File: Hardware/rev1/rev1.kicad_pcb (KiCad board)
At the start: 4 copper layers, 50 x 25 mm, 16 parts, among them J1 USB_C_Receptacle_GCT_USB4105-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, J3 TerminalBlock_MetzConnect_360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, U1 STM32F103C8Tx, U2 HT75xx-1-SOT89, U3 MS5607-02BA, U4 W25Q128JVS, Y1 16MHz

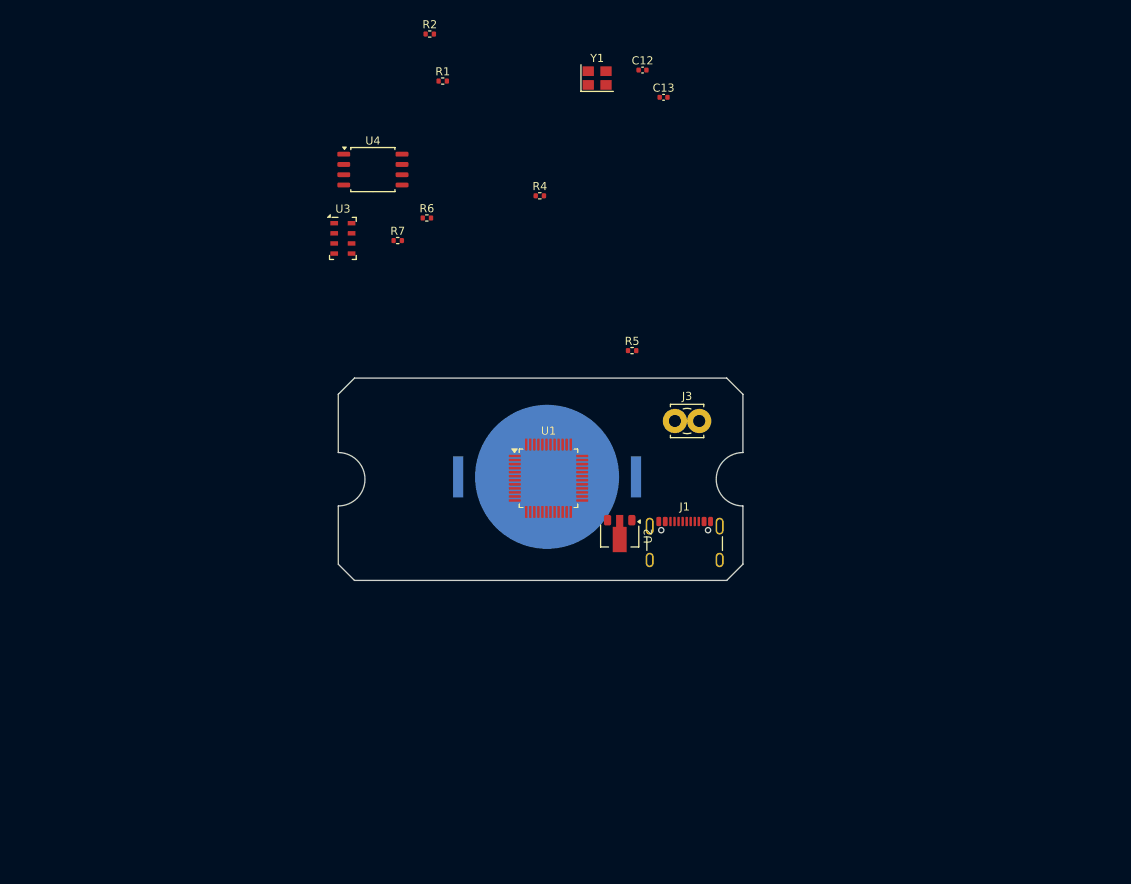
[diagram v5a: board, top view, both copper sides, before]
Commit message: Literal Progress
PCB populated, schematic changed, all pins on MCU accessible from headers, all components on board, traces required
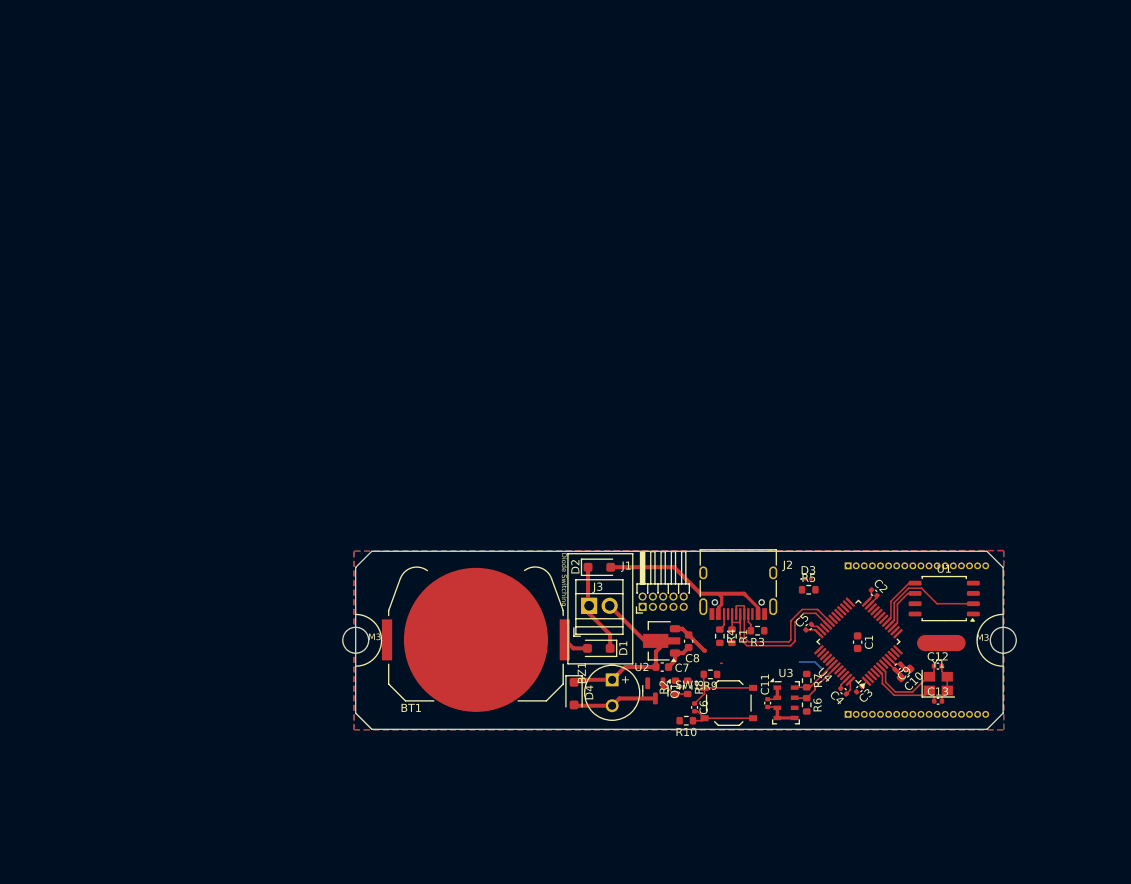
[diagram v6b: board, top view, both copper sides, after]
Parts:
- removed REF**: BatteryHolder_Keystone_3034_1x20mm, Battery:BatteryHolder_Keystone_3034_1x20mm
- added BT1: Battery_Cell, Battery:BatteryHolder_Keystone_3034_1x20mm, F.Cu at (128.0, 129.1)
- added BZ1: Buzzer, Buzzer_Beeper:MagneticBuzzer_Kingstate_KCG0601, F.Cu at (144.8, 134.1)
- added C1: 4.7u, Capacitor_SMD:C_0603_1608Metric, F.Cu at (175.2, 129.4)
- added C10: 1u, Capacitor_SMD:C_0603_1608Metric, F.Cu at (181.1, 133.3)
- added C11: 100n, Capacitor_SMD:C_0402_1005Metric, F.Cu at (164.1, 137.0)
- added C2: 100n, Capacitor_SMD:C_0402_1005Metric, F.Cu at (177.2, 123.3)
- added C3: 100n, Capacitor_SMD:C_0402_1005Metric, F.Cu at (175.4, 135.2)
- added C4: 100n, Capacitor_SMD:C_0402_1005Metric, F.Cu at (173.4, 135.5)
- added C5: 100n, Capacitor_SMD:C_0402_1005Metric, F.Cu at (169.1, 127.6)
- added C6: 100n, Capacitor_SMD:C_0402_1005Metric, F.Cu at (155.0, 137.5)
- added C7: 10u, Capacitor_SMD:C_0603_1608Metric, F.Cu at (151.0, 132.5)
- added C8: 10u, Capacitor_SMD:C_0603_1608Metric, F.Cu at (154.3, 129.3)
- added C9: 10n, Capacitor_SMD:C_0402_1005Metric, F.Cu at (180.1, 132.5)
- added D1: D, Diode_SMD:D_SOD-123F, F.Cu at (143.2, 130.2)
- added D2: D, Diode_SMD:D_SOD-123F, F.Cu at (143.3, 120.2)
- added D3: LED, LED_SMD:LED_0201_0603Metric, F.Cu at (169.1, 121.6)
- added D4: SM4007, Diode_SMD:D_SOD-123F, F.Cu at (140.1, 135.8)
- added H1: MountingHole, MountingHole:MountingHole_3.2mm_M3, F.Cu at (193.2, 129.2)
- added H2: MountingHole, MountingHole:MountingHole_3.2mm_M3, F.Cu at (113.2, 129.2)
- added J2: USB_C_Receptacle_USB2.0_14P, Connector_USB:USB_C_Receptacle_HRO_TYPE-C-31-M-12, F.Cu at (160.4, 121.9)
- added J4: Conn_01x18_Socket, Connector_PinHeader_1.00mm:PinHeader_1x18_P1.00mm_Vertical, B.Cu at (174.0, 120.0)
- added J5: Conn_01x18_Socket, Connector_PinHeader_1.00mm:PinHeader_1x18_P1.00mm_Vertical, B.Cu at (174.0, 138.3)
- added NT1: NetTie_2, NetTie:NetTie-2_SMD_Pad2.0mm, F.Cu at (185.5, 129.5)
- added Q1: AO3400A, Package_TO_SOT_SMD:SOT-23, F.Cu at (150.2, 135.4)
- added R10: 10k, Resistor_SMD:R_0603_1608Metric, F.Cu at (154.0, 139.1)
- added R3: 5k1, Resistor_SMD:R_0603_1608Metric, F.Cu at (162.8, 128.0)
- added R8: 10k, Resistor_SMD:R_0603_1608Metric, F.Cu at (154.2, 135.0)
- added R9: 1k, Resistor_SMD:R_0603_1608Metric, F.Cu at (157.0, 133.4)
- added SW1: SW_Push, Button_Switch_SMD:SW_Push_1P1T_XKB_TS-1187A, F.Cu at (159.3, 137.0)
- J1: value USB_C_Receptacle_GCT_USB4105-xx-A_16P_TopMnt_Horizontal -> Conn_ARM_JTAG_SWD_10; footprint Connector_USB:USB_C_Receptacle_GCT_USB4105-xx-A_16P_TopMnt_Horizontal -> Connector_PinHeader_1.27mm:PinHeader_2x05_P1.27mm_Horizontal
- J3: value TerminalBlock_MetzConnect_360272_1x01_Horizontal_ScrewM2.6 -> Screw_Terminal_01x02; footprint TerminalBlock_MetzConnect:TerminalBlock_MetzConnect_360272_1x01_Horizontal_ScrewM2.6 -> TerminalBlock:TerminalBlock_Xinya_XY308-2.54-2P_1x02_P2.54mm_Horizontal
- R1, R4, R6, R7: footprint Resistor_SMD:R_0402_1005Metric -> Resistor_SMD:R_0603_1608Metric
- R2: value 5k1 -> 270; footprint Resistor_SMD:R_0402_1005Metric -> Resistor_SMD:R_0603_1608Metric
- R5: value 1k5 -> 470R; footprint Resistor_SMD:R_0402_1005Metric -> Resistor_SMD:R_0603_1608Metric
- U1: value STM32F103C8Tx -> W25Q128JVS; footprint Package_QFP:LQFP-48_7x7mm_P0.5mm -> Package_SO:SOIC-8_5.23x5.23mm_P1.27mm
- U4: value W25Q128JVS -> STM32F103C8Tx; footprint Package_SO:SOIC-8_5.23x5.23mm_P1.27mm -> Package_QFP:LQFP-48_7x7mm_P0.5mm
- moved R2 86.2 mm to (152.7, 135.0), turned to 90 degrees
- moved Y1 85.9 mm to (185.1, 134.6)
- moved U4 83.7 mm to (175.3, 129.4), turned to 135 degrees
- moved C12 82.2 mm to (185.1, 132.4)
- moved C13 82.0 mm to (185.1, 136.7)
- moved U3 79.3 mm to (166.3, 136.9)
- moved R1 77.4 mm to (159.6, 128.7), turned to -90 degrees
- moved R6 76.3 mm to (168.9, 137.2), turned to 90 degrees
- moved R7 74.2 mm to (168.9, 134.2), turned to -90 degrees
- moved R4 58.8 mm to (158.1, 128.7), turned to -90 degrees
- moved U1 51.1 mm to (185.9, 124.0), turned to 180 degrees
- moved R5 36.7 mm to (169.1, 123.0)
- moved J3 25.2 mm to (142.0, 124.9)
- moved U2 13.9 mm to (150.7, 129.3), turned to 180 degrees
- moved J1 8.61 mm to (148.6, 125.1), turned to 90 degrees
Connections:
- C12 pad 1: HSE_OUT -> /Microcontroller/HSE_OUT
- C13 pad 1: HSE_IN -> /Microcontroller/HSE_IN
- J3 pad 1: (no net) -> Net-(D1-K)
- R1 pad 1: D+ -> /Microcontroller/USB.D+
- R2 pad 1: GND -> Net-(Q1-G)
- R2 pad 2: Net-(J1-CC1) -> /Microcontroller/BUZZER
- R6 pad 2: I2C2_SDA -> /Microcontroller/I2C2.SDA
- R7 pad 2: I2C2_SCK -> /Microcontroller/I2C2.SCK
- U1 pad 1: +3.3V -> unconnected-(U1-~{CS}-Pad1)
- U1 pad 2: unconnected-(U1-PC13-Pad2) -> /Microcontroller/SPI1.MISO
- U1 pad 4: unconnected-(U1-PC15-Pad4) -> GND
- U1 pad 5: HSE_IN -> /Microcontroller/SPI1.MOSI
- U1 pad 6: HSE_OUT -> /Microcontroller/SPI1.SCLK
- U1 pad 7: /MCU et al Sheet/System_Reset -> unconnected-(U1-IO3-Pad7)
- U1 pad 8: GND -> +3.3V
- U2 pad 2: Net-(J3-Pin_2) -> VBUS
- U2 pad 3: +3V3 -> +3.3V
- U3 pad 7: I2C2_SDA -> /Microcontroller/I2C2.SDA
- U3 pad 8: I2C2_SCK -> /Microcontroller/I2C2.SCK
- U4 pad 1: unconnected-(U4-~{CS}-Pad1) -> +3.3V
- U4 pad 2: Flash Data Out -> /Microcontroller/PC13
- U4 pad 3: unconnected-(U4-IO2-Pad3) -> /Microcontroller/PC14
- U4 pad 4: GND -> /Microcontroller/PC15
- U4 pad 5: Flash Data In -> /Microcontroller/HSE_IN
- U4 pad 6: SPI_CLK -> /Microcontroller/HSE_OUT
- U4 pad 7: unconnected-(U4-IO3-Pad7) -> /Microcontroller/DBG.NRESET
- U4 pad 8: +3.3V -> GND
- Y1 pad 1: HSE_IN -> /Microcontroller/HSE_IN
- Y1 pad 4: HSE_OUT -> /Microcontroller/HSE_OUT
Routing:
- net VBUS: track 0.00 -> 25.4 mm
- net VUSB: track 0.00 -> 23.9 mm
- net /Microcontroller/USB.D+: track 0.00 -> 22.8 mm
- net GND: track 0.00 -> 21.1 mm
- net /Microcontroller/USB.D-: track 0.00 -> 20.4 mm
- net /Microcontroller/SPI1.MISO: track 0.00 -> 14.3 mm
- net +3.3V: track 0.00 -> 13.5 mm
- net Net-(D1-K): track 0.00 -> 11.4 mm
- net /Microcontroller/HSE_IN: track 0.00 -> 10.6 mm
- net /Microcontroller/HSE_OUT: track 0.00 -> 10.5 mm
- net Net-(BZ1--): track 0.00 -> 10.5 mm
- net Net-(C6-Pad1): track 0.00 -> 10.1 mm
- net /Microcontroller/DBG.NRESET: track 0.00 -> 9.34 mm
- net /Microcontroller/I2C2.SDA: track 0.00 -> 7.05 mm
- net /Microcontroller/SPI1.MOSI: track 0.00 -> 6.71 mm
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- added copper zone on B.Cu, net GND
- added copper zone on F.Cu, net GND
- added copper zone on In1.Cu, net GND
- added copper zone on In2.Cu, net GND
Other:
- board size 50 x 25 mm -> 80 x 22 mm
- board text added: "Diode Switching"
- board text added: "M3"

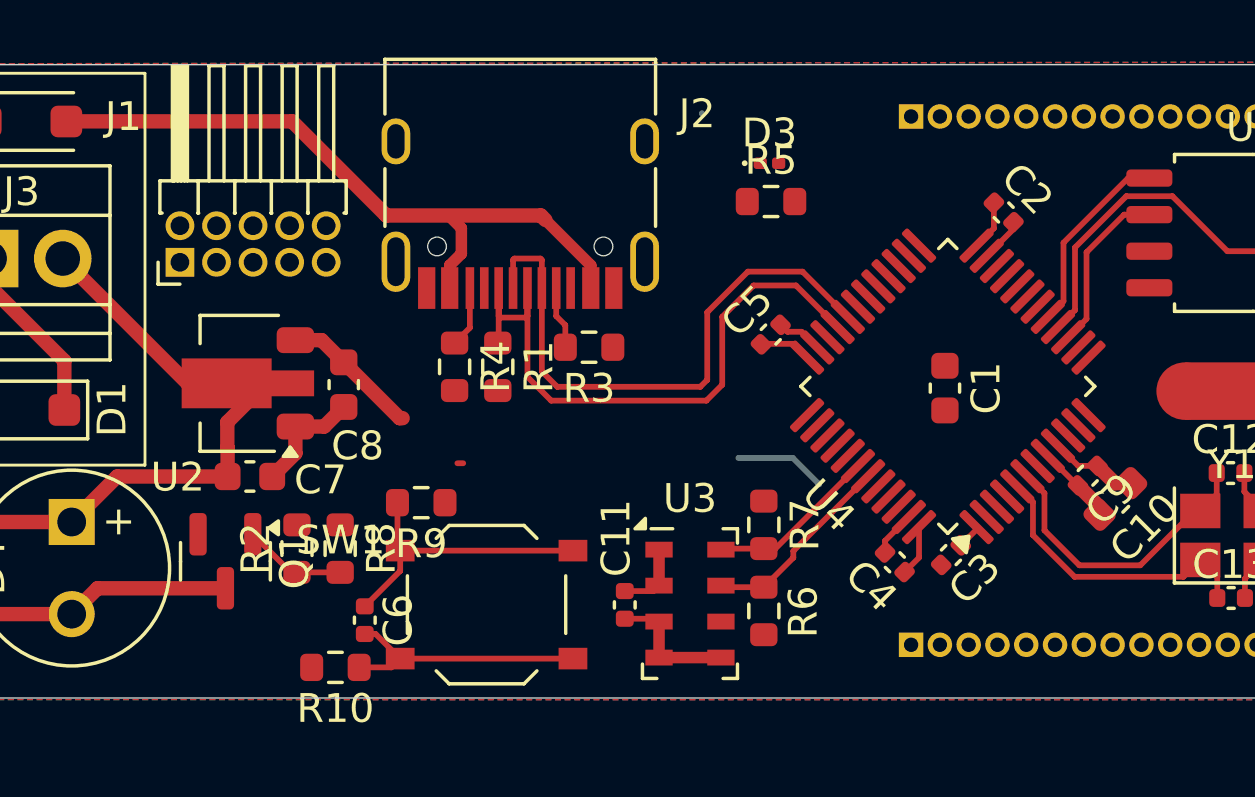
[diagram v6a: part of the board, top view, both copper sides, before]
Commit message: Added traces ont back
Still need to fix the header pin labels on schematic
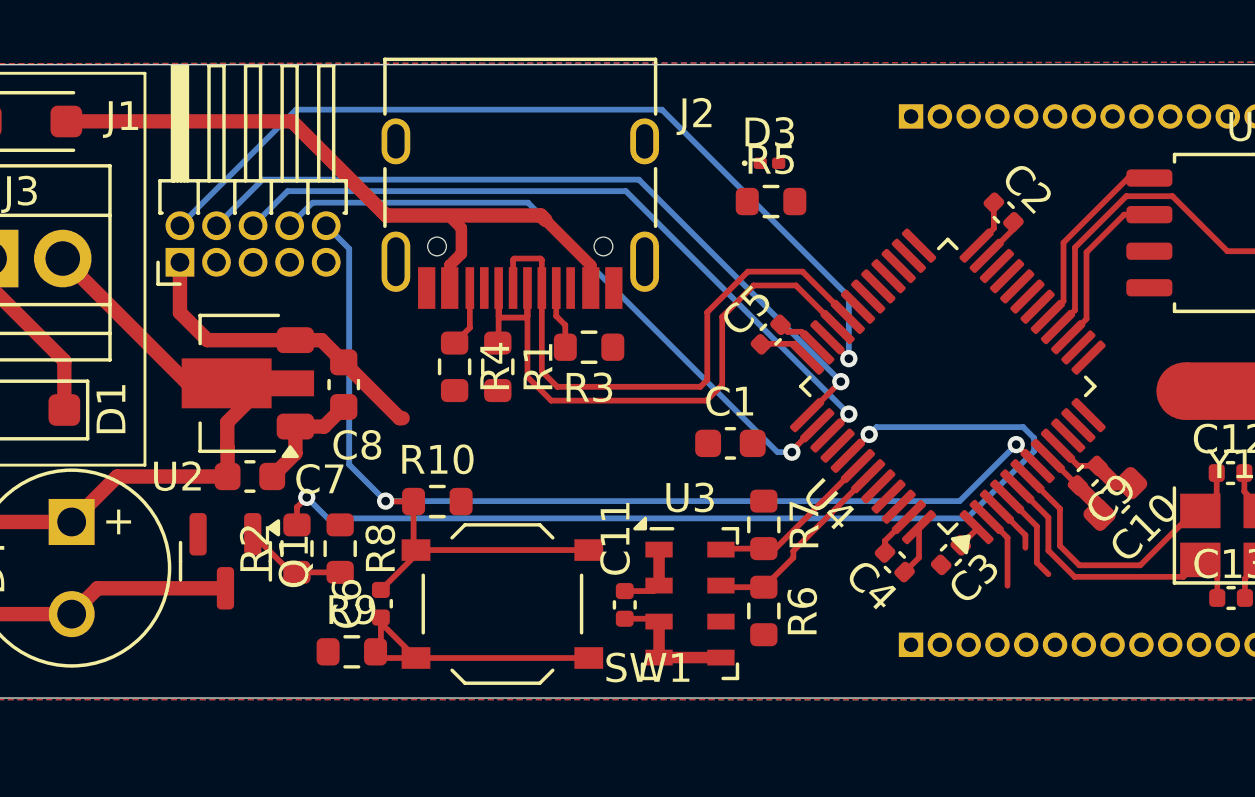
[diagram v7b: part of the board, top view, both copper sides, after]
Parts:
- moved C1 7.69 mm to (167.7, 131.4), turned to 0 degrees
- moved R10 6.76 mm to (157.5, 133.4), turned to 0 degrees
- moved R9 5.71 mm to (154.6, 138.6), turned to 0 degrees
- moved C6 0.80 mm to (155.6, 136.9), turned to 90 degrees
- moved SW1 0.55 mm to (159.8, 136.9), turned to 180 degrees
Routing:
- net /Microcontroller/DBG.NRESET: track 9.34 -> 44.8 mm, vias 0 -> 2
- net /Microcontroller/BUZZER: track 3.19 -> 35.1 mm, vias 0 -> 2
- net /Microcontroller/DBG.TMS/SWDIO: track 0.00 -> 30.8 mm, vias 0 -> 1
- net /Microcontroller/DBG.JTCK/SWCLK: track 0.00 -> 26.9 mm, vias 0 -> 1
- net /Microcontroller/DBG.JTDO/SWO: track 0.00 -> 25.4 mm, vias 0 -> 1
- net /Microcontroller/DBG.JTDI/NC: track 0.00 -> 22.7 mm, vias 0 -> 1
- net +3.3V: track 13.5 -> 19.7 mm
- net /Microcontroller/PC15: track 0.00 -> 3.29 mm
- net /Microcontroller/PC13: track 0.00 -> 2.69 mm
- net /Microcontroller/PC14: track 0.00 -> 1.83 mm
- net Net-(C6-Pad1): track 10.1 -> 10.7 mm
